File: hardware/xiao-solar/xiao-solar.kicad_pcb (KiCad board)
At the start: 2 copper layers, 48 x 71.5 mm, 73 parts, among them J1 SOLAR, J2 VIN2 5-20V, J3 NTC 10k (103AT), J4 BATTERY, J5 I2C rail, Q2 AO3400A (ship FET), Q3 HJ8205, U1 BQ25798RQMR, U2 DW01A, U3 XIAO nRF52840, U4 Wio-SX1262 for XIAO, U5 SHT40-AD1B, U7 INA219AIDCNR

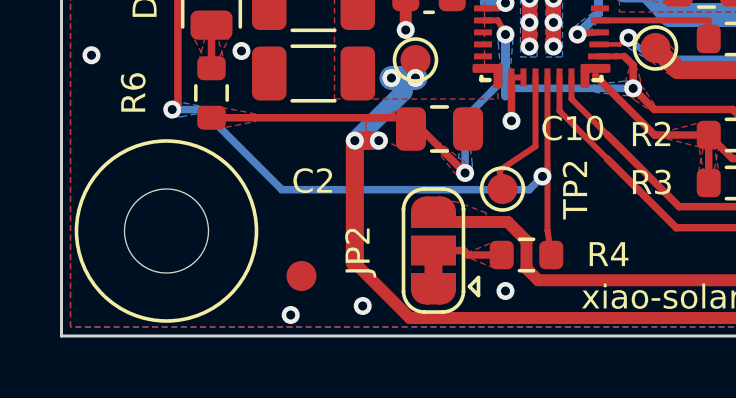
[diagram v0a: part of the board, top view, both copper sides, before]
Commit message: hardware: fiducial clearance 0.65 mm so the GND pour stays under mask (JLC DFM), move one GND via
Co-Authored-By: Claude Opus 5.5 <noreply@anthropic.com>
Claude-Session: https://claude.ai/code/session_01P5Km81NY9NPL6RpKFGVEbH
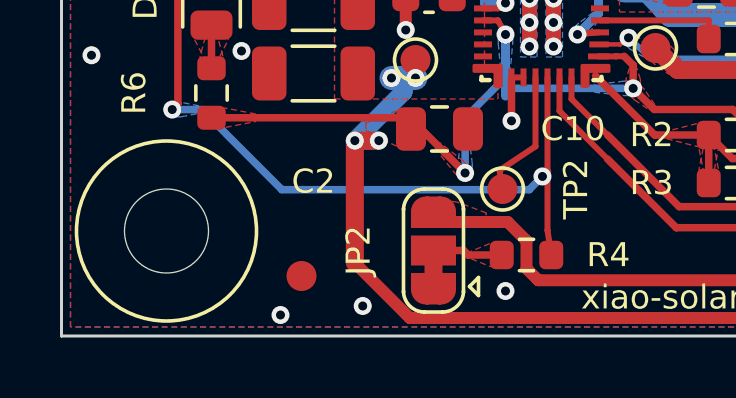
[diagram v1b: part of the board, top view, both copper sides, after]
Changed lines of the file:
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@@
       (stroke (width 0.1) (type solid)) (fill none) (layer "F.Fab"))
     (pad "" smd circle (at 0 0) (size 1 1) (layers "F.Cu" "F.Mask")
-      (solder_mask_margin 0.5) (clearance 0.5))
+      (solder_mask_margin 0.5) (clearance 0.65))
   )
   (footprint "xiao_solar:SOT-23-6_L2.9-W1.6-P0.95-LS2.8-BL" (layer "F.Cu")
@@
       (stroke (width 0.1) (type solid)) (fill none) (layer "F.Fab"))
     (pad "" smd circle (at 0 0) (size 1 1) (layers "F.Cu" "F.Mask")
-      (solder_mask_margin 0.5) (clearance 0.5))
+      (solder_mask_margin 0.5) (clearance 0.65))
   )
   (footprint "Capacitor_SMD:C_0805_2012Metric" (layer "F.Cu")
@@
       (stroke (width 0.1) (type solid)) (fill none) (layer "F.Fab"))
     (pad "" smd circle (at 0 0) (size 1 1) (layers "F.Cu" "F.Mask")
-      (solder_mask_margin 0.5) (clearance 0.5))
+      (solder_mask_margin 0.5) (clearance 0.65))
   )
   (footprint "TestPoint:TestPoint_Pad_D1.0mm" (layer "F.Cu")
@@
   (via (at 130.283 122.283) (size 0.6) (drill 0.3) (layers "F.Cu" "B.Cu") (net 2))
   (via (at 126 126) (size 0.6) (drill 0.3) (layers "F.Cu" "B.Cu") (net 2))
-  (via (at 107.641 170.8) (size 0.6) (drill 0.3) (layers "F.Cu" "B.Cu") (net 2))
+  (via (at 107.3 170.8) (size 0.6) (drill 0.3) (layers "F.Cu" "B.Cu") (net 2))
   (via (at 121 104) (size 0.6) (drill 0.3) (layers "F.Cu" "B.Cu") (net 2))
   (via (at 121.717 129.717) (size 0.6) (drill 0.3) (layers "F.Cu" "B.Cu") (net 2))
